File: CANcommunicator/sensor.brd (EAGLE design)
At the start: 33 x 26.2 mm, 31 parts, among them U1 ATSAMC21E18A-AU, U2 MCP2551

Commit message: Make ground plane better cover some analog inputs
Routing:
- net S01: track 16.6 -> 16.0 mm
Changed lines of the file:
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@@
 <contactref element="SENSOR" pad="3"/>
 <via x="11.049" y="12.573" extent="1-16" drill="0.35"/>
+<via x="22.987" y="12.954" extent="1-16" drill="0.35"/>
+<via x="25.527" y="13.081" extent="1-16" drill="0.35"/>
+<via x="27.813" y="14.732" extent="1-16" drill="0.35"/>
+<via x="28.448" y="13.081" extent="1-16" drill="0.35"/>
+<via x="27.94" y="17.399" extent="1-16" drill="0.35"/>
 </signal>
 <signal name="CAN1H">
@@
 <wire x1="16.11" y1="8.4074" x2="16.3766" y2="8.1408" width="0.2032" layer="1"/>
 <wire x1="16.3766" y1="8.1408" x2="16.3766" y2="7.6671875" width="0.2032" layer="1"/>
-<wire x1="16.3766" y1="7.6671875" x2="18.9637875" y2="5.08" width="0.2032" layer="1"/>
-<wire x1="29.21" y1="5.08" x2="30.48" y2="6.35" width="0.2032" layer="1"/>
-<wire x1="29.21" y1="5.08" x2="18.9637875" y2="5.08" width="0.2032" layer="1"/>
+<wire x1="16.3766" y1="7.6671875" x2="18.3287875" y2="5.715" width="0.2032" layer="1"/>
+<wire x1="29.845" y1="5.715" x2="30.48" y2="6.35" width="0.2032" layer="1"/>
+<wire x1="29.845" y1="5.715" x2="18.3287875" y2="5.715" width="0.2032" layer="1"/>
 </signal>
 <signal name="S02">

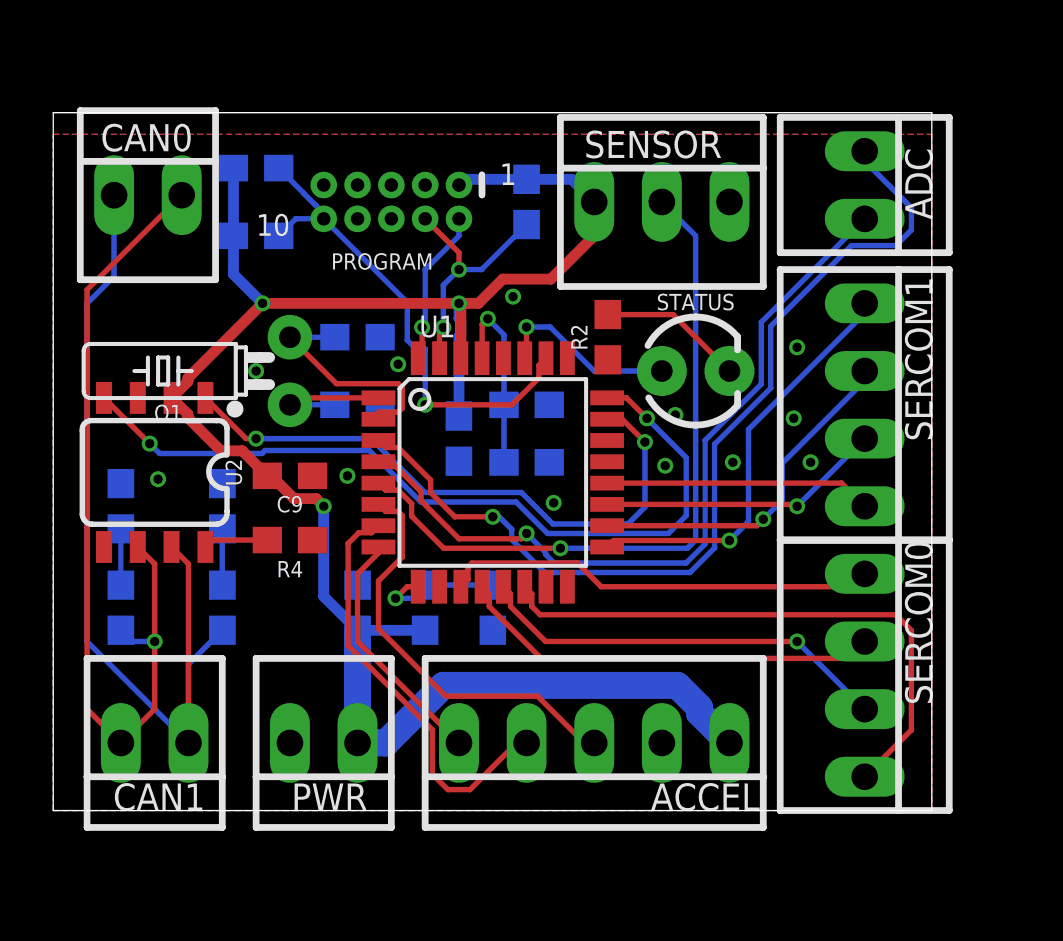
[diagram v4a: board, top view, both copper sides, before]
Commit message: moved some decoupling caps
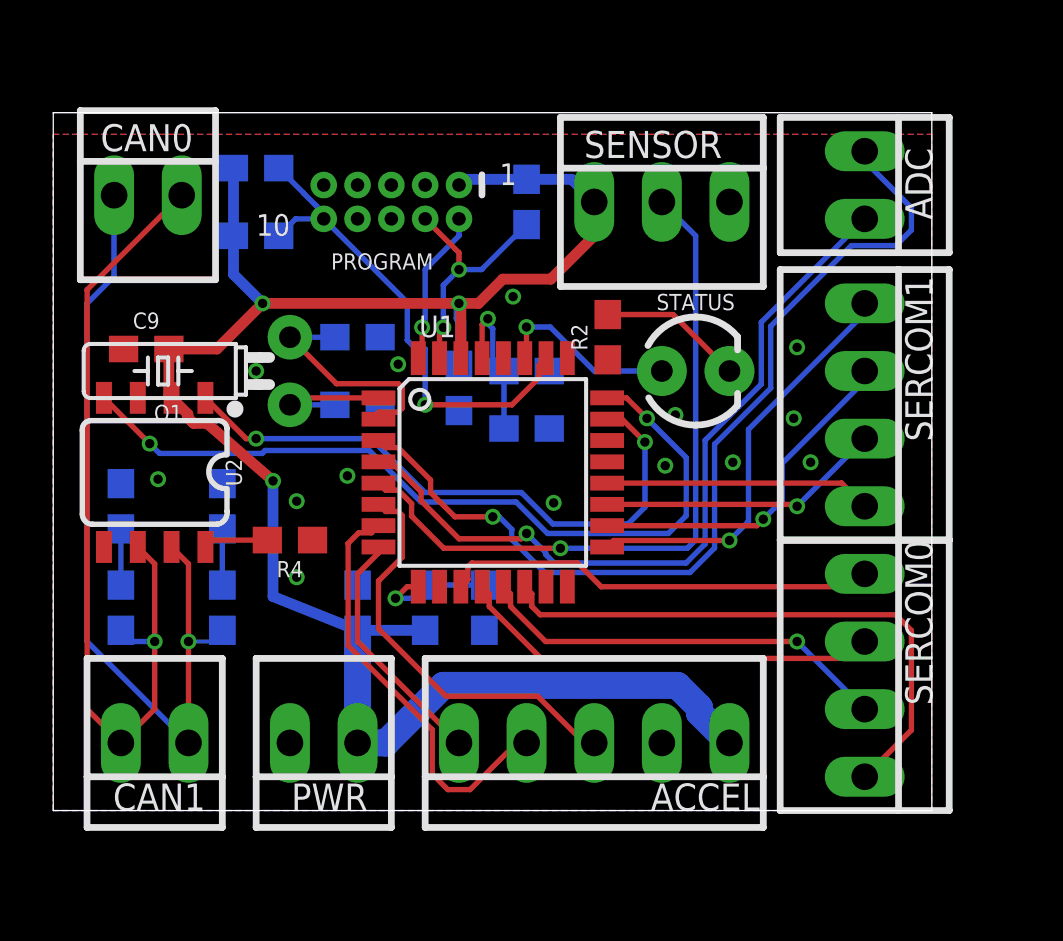
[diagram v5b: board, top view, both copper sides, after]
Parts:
- moved C9 7.20 mm to (3.49, 17.3), turned to 0 degrees
- moved C3 1.90 mm to (15.2, 15.9)
- moved C4 1.27 mm to (17.8, 16.5)
- moved C5 1.27 mm to (17.8, 14.4)
- moved C2 0.32 mm to (16.2, 7.62)
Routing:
- net CAN1H: track 35.0 -> 31.6 mm, vias 0 -> 1
- net VDDCORE: track 7.21 -> 6.00 mm
- net VCC: track 72.5 -> 71.9 mm

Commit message: moved some stuff
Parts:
- moved C5 0.71 mm to (18.1, 15.0)
- moved C9 0.64 mm to (3.49, 18.0)
- moved C4 0.45 mm to (18.1, 16.8)

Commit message: Revert changes in sensor.brd
The file in this branch is out of date and will break when we try
to merge otherwise.
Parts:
- moved C5 0.71 mm to (17.8, 14.4)
- moved C9 0.64 mm to (3.49, 17.3)
- moved C4 0.45 mm to (17.8, 16.5)

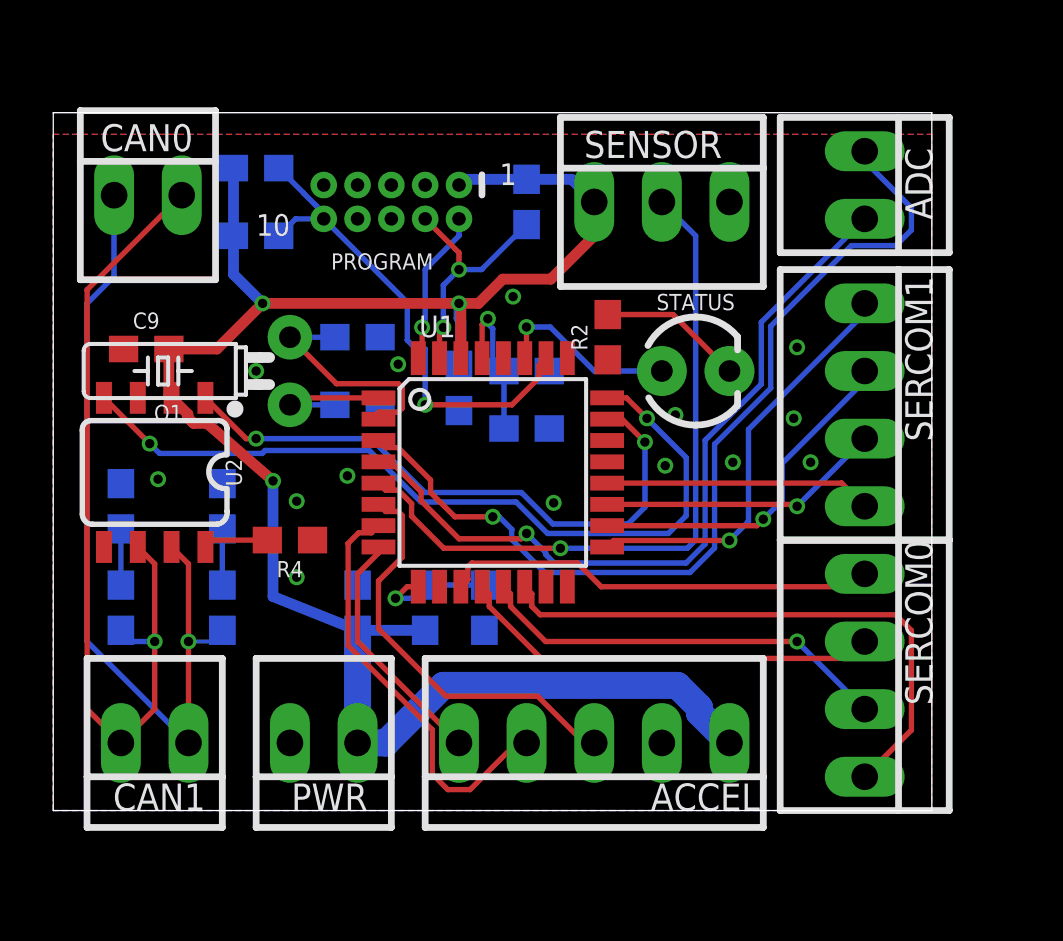
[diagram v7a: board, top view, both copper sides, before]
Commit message: Fix insanely obvious error in CAN interface
VSS means GROUND, VDD means POWER
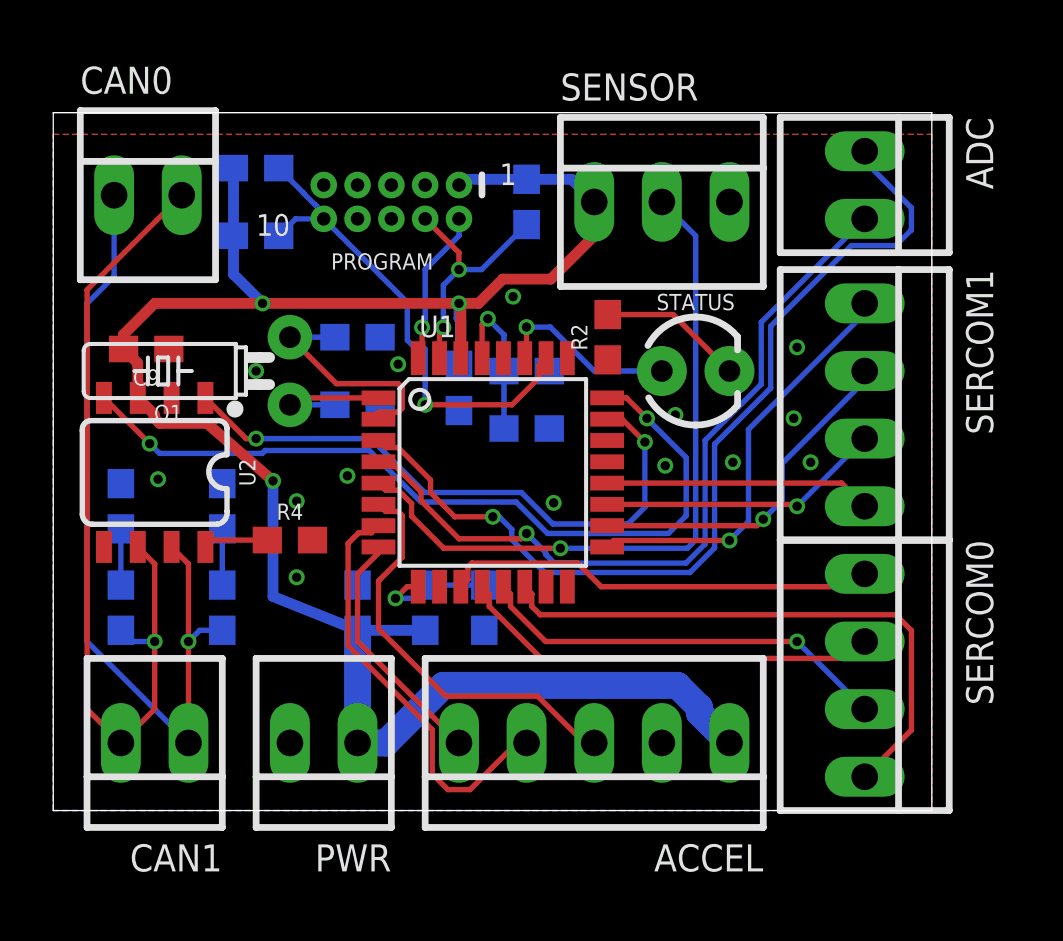
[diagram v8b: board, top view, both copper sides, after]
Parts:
- turned C9 to 180 degrees
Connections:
- net GND: now also U2.2; no longer U2.3
- net VCC: now also U2.3; no longer U2.2
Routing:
- net VCC: track 71.9 -> 75.4 mm
